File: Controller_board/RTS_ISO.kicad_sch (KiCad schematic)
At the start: 18 parts, among them U7 ADuM1400xRW, U8 ADuM1400xRW, U9 ADuM1400xRW

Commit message: Modify Digit_IN, Motherbord, Step motors, photo
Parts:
- U7, U8, U9: value ADuM1400xRW -> ADuM1400xRW SOIC-16W
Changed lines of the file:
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@@
       (effects (font (size 1.27 1.27)))
     )
-    (property "Value" "ADuM1400xRW" (at 113.03 148.59 0)
+    (property "Value" "ADuM1400xRW SOIC-16W" (at 113.03 148.59 0)
       (effects (font (size 1.27 1.27)))
     )
@@
       (effects (font (size 1.27 1.27)))
     )
-    (property "Value" "ADuM1400xRW" (at 113.03 93.98 0)
+    (property "Value" "ADuM1400xRW SOIC-16W" (at 113.03 93.98 0)
       (effects (font (size 1.27 1.27)))
     )
@@
       (effects (font (size 1.27 1.27)))
     )
-    (property "Value" "ADuM1400xRW" (at 114.3 35.56 0)
-      (effects (font (size 1.27 1.27)))
-    )
+    (property "Value" "ADuM1400xRW SOIC-16W" (at 114.3 35.56 0)
+      (effects (font (size 1.27 1.27)))
+    )

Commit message: Modify MainController Schems and PCB1
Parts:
- added R19, R20, R21, R22, R23, R24, R25, R26, R27, R28, R29, R30: 103 0603, PCM_4ms_Resistor:R_0603, symbol Device:R
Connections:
- net GNDD: now also R19.2, R20.2, R21.2, R22.2, R23.2, R24.2, R25.2, R26.2, R27.2, R28.2, R29.2, R30.2
- net RTS10_cont: now also R21.1
- net RTS11_cont: now also R20.1
- net RTS12_cont: now also R19.1
- net RTS1_cont: now also R30.1
- net RTS2_cont: now also R29.1
- net RTS3_cont: now also R28.1
- net RTS4_cont: now also R27.1
- net RTS5_cont: now also R26.1
- net RTS6_cont: now also R25.1
- net RTS7_cont: now also R24.1
- net RTS8_cont: now also R23.1
- net RTS9_cont: now also R22.1
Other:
- moved on the sheet: C50, C54, R14, R15, R16, U7, U8, U9

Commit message: Change ISOLATOR 03.06.24
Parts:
- removed U7, U8, U9: ADuM1400xRW SOIC-16W, Package_SO:SOIC-16W_7.5x10.3mm_P1.27mm, symbol Isolator:ADuM1400xRW
- added U4, U7, U8: π140M3x, Package_SO:SOIC-16_3.9x9.9mm_P1.27mm, symbol Isolator:π140M3x
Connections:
- net +3.3VRS485: now also U4.1 (VDD1), U7.1 (VDD1), U8.1 (VDD1)
- net +5V: now also U4.16 (VDD2), U7.16 (VDD2), U8.16 (VDD2)
- net GND1: now also U4.2 (GND1), U4.8 (GND1), U7.2 (GND1), U7.8 (GND1), U8.2 (GND1), U8.8 (GND1)
- net GNDD: now also U4.15 (GND2), U4.9 (GND2), U7.15 (GND2), U7.9 (GND2), U8.15 (GND2), U8.9 (GND2)
- net RTS1: now also R30.1, U4.3 (VIA)
- net RTS10: now also R21.1, U8.4 (VIB)
- net RTS10_cont: now also U8.13 (VOB); no longer R21.1
- net RTS11: now also R20.1, U8.5 (VIC)
- net RTS11_cont: now also U8.12 (VOC); no longer R20.1
- net RTS12: now also R19.1, U8.6 (VID)
- net RTS12_cont: now also U8.11 (VOD); no longer R19.1
- net RTS1_cont: now also U4.14 (VOA); no longer R30.1
- net RTS2: now also R29.1, U4.4 (VIB)
- net RTS2_cont: now also U4.13 (VOB); no longer R29.1
- net RTS3: now also R28.1, U4.5 (VIC)
- net RTS3_cont: now also U4.12 (VOC); no longer R28.1
- net RTS4: now also R27.1, U4.6 (VID)
- net RTS4_cont: now also U4.11 (VOD); no longer R27.1
- net RTS5: now also R26.1, U7.3 (VIA)
- net RTS5_cont: now also U7.14 (VOA); no longer R26.1
- net RTS6: now also R25.1, U7.4 (VIB)
- net RTS6_cont: now also U7.13 (VOB); no longer R25.1
- net RTS7: now also R24.1, U7.5 (VIC)
- net RTS7_cont: now also U7.12 (VOC); no longer R24.1
- net RTS8: now also R23.1, U7.6 (VID)
- net RTS8_cont: now also U7.11 (VOD); no longer R23.1
- net RTS9: now also R22.1, U8.3 (VIA)
- net RTS9_cont: now also U8.14 (VOA); no longer R22.1
- net at R16.2: now also U8.10 (VE2)
- net at R15.2: now also U7.10 (VE2)
- net at R14.2: now also U4.10 (VE2)
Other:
- moved on the sheet: C50, C54, R14, R15, R16, R19, R20, R21, R22, R23, R24, R25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

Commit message: pcb and schems main controller 07.06.24
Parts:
- added TP1, TP10, TP11, TP12, TP13, TP14, TP15, TP16, TP17, TP18, TP19, TP2, TP20, TP21, TP22, TP23, TP24, TP3, TP4, TP5, TP6, TP7, TP8, TP9: TestPoint, PCM_4ms_TestPoint:TestPoint_D1, symbol Connector:TestPoint
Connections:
- net GND1: now also R19.2, R20.2, R21.2, R22.2, R23.2, R24.2, R25.2, R26.2, R27.2, R28.2, R29.2, R30.2
- net GNDD: no longer R19.2, R20.2, R21.2, R22.2, R23.2, R24.2, R25.2, R26.2, R27.2, R28.2, R29.2, R30.2
- net RTS1: now also TP13.1
- net RTS10: now also TP22.1
- net RTS10_cont: now also TP10.1
- net RTS11: now also TP23.1
- net RTS11_cont: now also TP11.1
- net RTS12: now also TP24.1
- net RTS12_cont: now also TP12.1
- net RTS1_cont: now also TP1.1
- net RTS2: now also TP14.1
- net RTS2_cont: now also TP2.1
- net RTS3: now also TP15.1
- net RTS3_cont: now also TP3.1
- net RTS4: now also TP16.1
- net RTS4_cont: now also TP4.1
- net RTS5: now also TP17.1
- net RTS5_cont: now also TP5.1
- net RTS6: now also TP18.1
- net RTS6_cont: now also TP6.1
- net RTS7: now also TP19.1
- net RTS7_cont: now also TP7.1
- net RTS8: now also TP20.1
- net RTS8_cont: now also TP8.1
- net RTS9: now also TP21.1
- net RTS9_cont: now also TP9.1
- net +3.3VRS485 renamed +3.3V

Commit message: Main controller renew schems and PCB
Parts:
- U4, U7, U8: value π140M3x -> π140M30 (SOIC-16)
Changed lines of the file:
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@@
       (effects (font (size 1.27 1.27)))
     )
-    (property "Value" "π140M3x" (at 130.81 30.48 0)
+    (property "Value" "π140M30 (SOIC-16)" (at 130.81 30.48 0)
       (effects (font (size 1.27 1.27)))
     )
@@
       (effects (font (size 1.27 1.27)))
     )
-    (property "Value" "π140M3x" (at 129.54 80.01 0)
+    (property "Value" "π140M30 (SOIC-16)" (at 129.54 80.01 0)
       (effects (font (size 1.27 1.27)))
     )
@@
       (effects (font (size 1.27 1.27)))
     )
-    (property "Value" "π140M3x" (at 129.54 129.54 0)
-      (effects (font (size 1.27 1.27)))
-    )
+    (property "Value" "π140M30 (SOIC-16)" (at 129.54 129.54 0)
+      (effects (font (size 1.27 1.27)))
+    )

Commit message: renew all schems and pcb for production
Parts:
- C50: footprint PCM_Resistor_SMD_AKL:R_0805_2012Metric_Pad1.20x1.40mm_HandSolder -> PCM_Capacitor_SMD_AKL:C_0805_2012Metric_Pad1.18x1.45mm_HandSolder
- R14, R15, R16: value 101 0805 -> 0805-100 Ом±5%-0,125 Вт
- R19, R20, R21, R22, R23, R24, R25, R26, R27, R28, R29, R30: value 103 0603 -> 0603-10 кОм±5%-0,062 Вт
- TP1, TP10, TP11, TP12, TP13, TP14, TP15, TP16, TP17, TP18, TP19, TP2, TP20, TP21, TP22, TP23, TP24, TP3, TP4, TP5, TP6, TP7, TP8, TP9: now left out of the parts list
- U4, U7, U8: value π140M30 (SOIC-16) -> pia140M30 (SOIC-16)

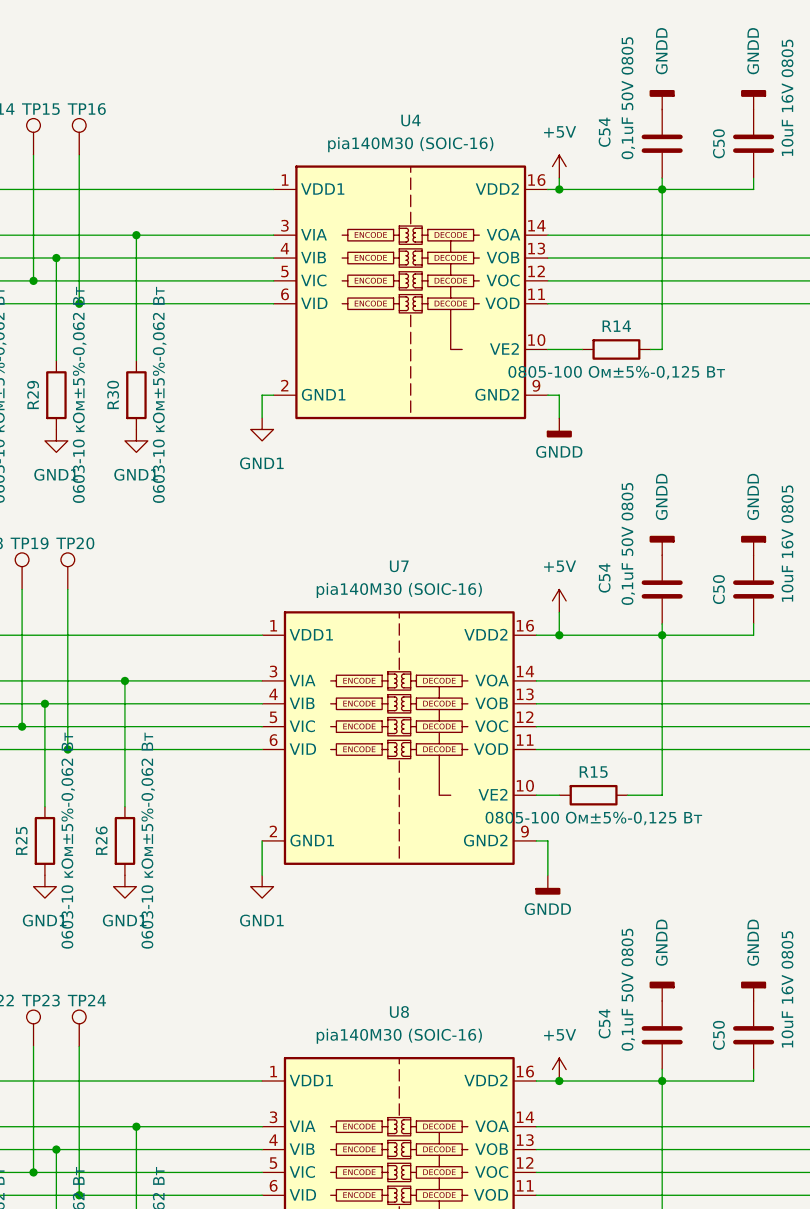
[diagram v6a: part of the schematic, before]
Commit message: fix "pia" typo
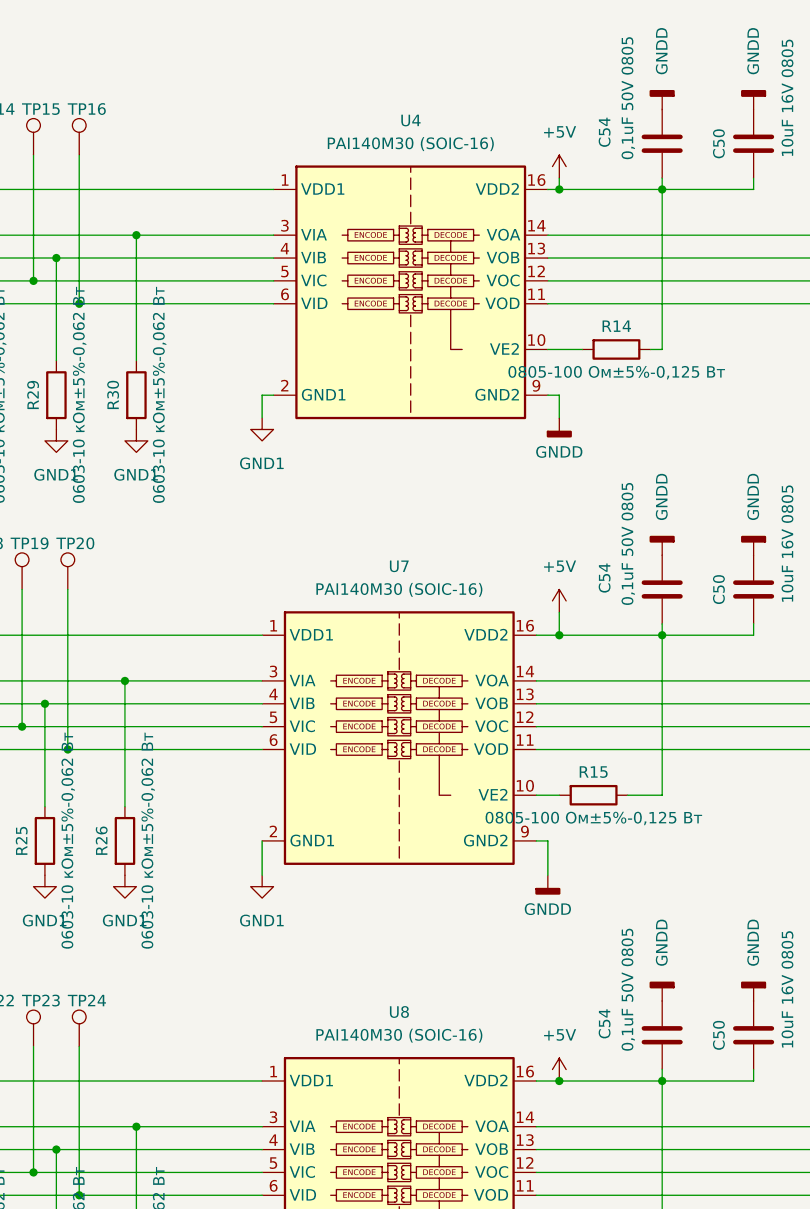
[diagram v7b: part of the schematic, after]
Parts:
- U4, U7, U8: value pia140M30 (SOIC-16) -> PAI140M30 (SOIC-16)
